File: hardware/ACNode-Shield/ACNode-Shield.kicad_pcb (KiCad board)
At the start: 2 copper layers, 50 x 50 mm, 15 parts, among them J1 MICRO_SD_HINGE, P1 CONN_NFC, P2 CONN_RELAY, P3 CONN_RGB_LED, P4 CONN_X6, P5 CONN_X7, P6 CONN_WS2812, Q1 PN2222A, SW1 SW_RST, SW2 SW_BTN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

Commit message: Rev 2 off to the fab
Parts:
- added CON1: SD_Card, SD_Slots:SD_Slot, F.Cu at (36.8, 49.5)
- C1: moved to F.Cu
- P2: footprint Pin_Headers:Pin_Header_Straight_1x03 -> Terminal_Blocks:TerminalBlock_Pheonix_MKDS1.5-3pol
- moved U2 11.8 mm to (58.0, 53.2), turned to 180 degrees
- moved P6 6.90 mm to (53.0, 54.0), turned to 180 degrees
- moved D1 6.41 mm to (32.0, 15.0)
- moved P2 5.78 mm to (15.0, 16.0), turned to 0 degrees
- moved C1 5.23 mm to (36.5, 40.0)
- moved U1 3.04 mm to (37.0, 29.5)
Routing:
- net +5V: track 129.1 -> 88.6 mm, vias 0 -> 1
- net PM7: track 17.1 -> 23.1 mm
- net PQ3: track 39.2 -> 44.8 mm, vias 0 -> 1
- net PQ1: track 41.3 -> 46.7 mm, vias 0 -> 1
- net PQ2: track 34.5 -> 39.5 mm, vias 0 -> 1
- net Net-(P2-Pad2): track 27.7 -> 22.9 mm
- net Net-(P6-Pad2): track 5.26 -> 9.67 mm
- net (no net): track 0.00 -> 3.17 mm
- net Net-(P2-Pad1): track 7.86 -> 10.9 mm
- net PQ0: track 31.7 -> 34.6 mm, vias 0 -> 2
- net Net-(D1-Pad2): track 29.9 -> 27.2 mm
- net +3.3v: track 52.4 -> 54.7 mm
- net GND: track 117.7 -> 119.5 mm, vias 0 -> 1
- net Net-(P2-Pad3): track 22.0 -> 21.1 mm
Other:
- board text added: "LHS ACNode Shield rev 2"
- board text removed: "LHS ACNode Shield rev 1"

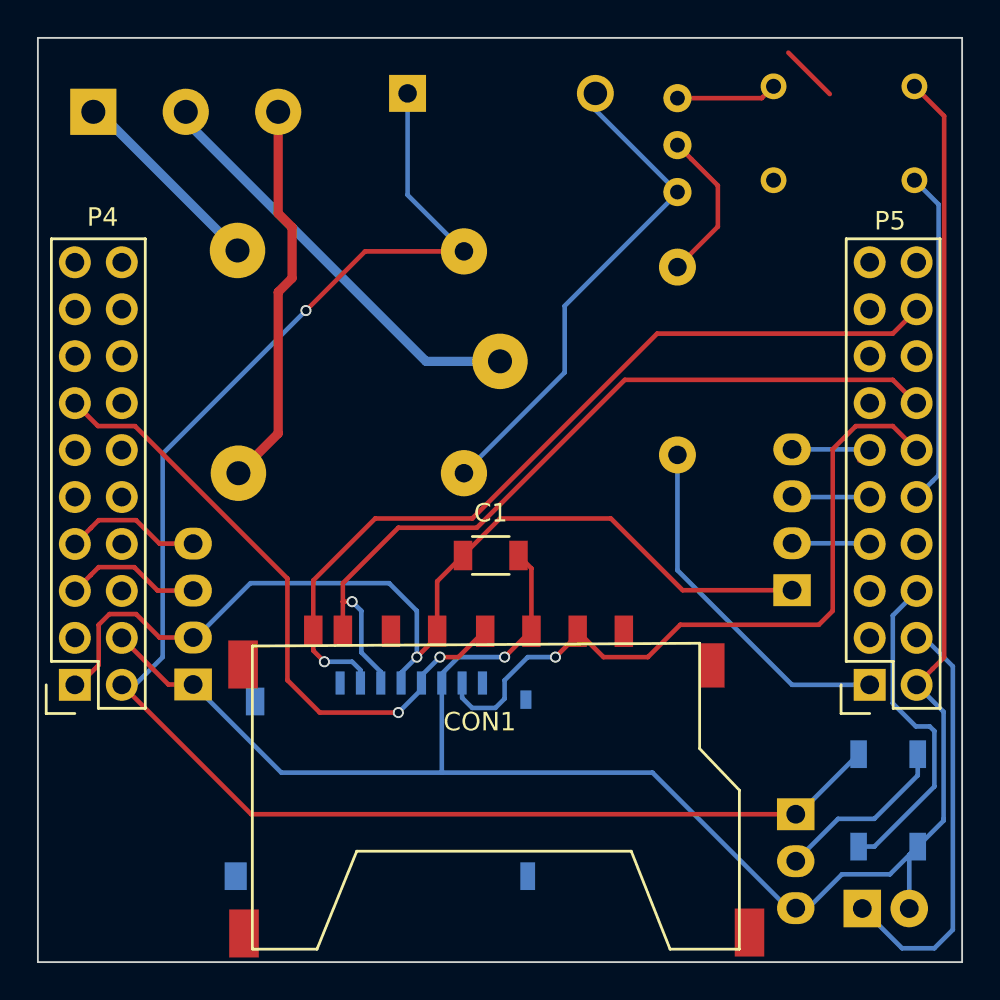
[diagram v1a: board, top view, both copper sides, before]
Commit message: Updated via outlines to be 1.2mm for easier manufacture.
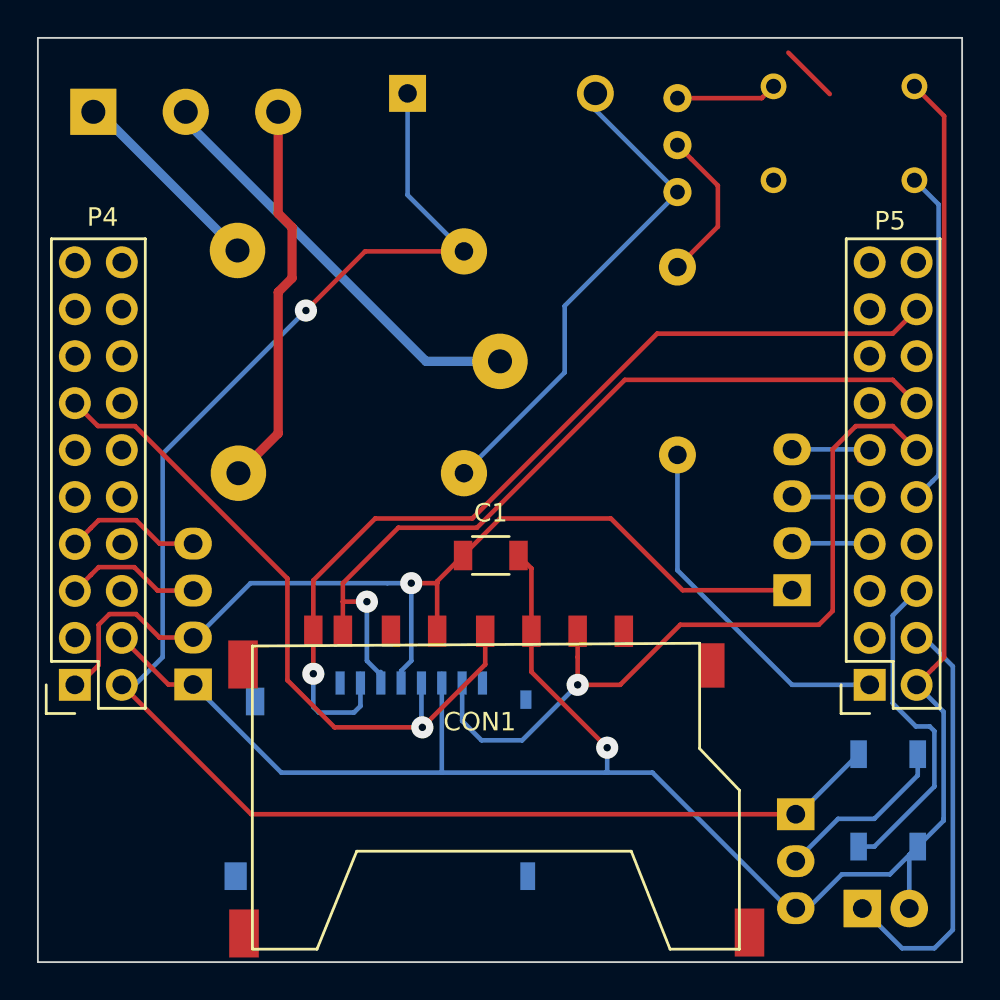
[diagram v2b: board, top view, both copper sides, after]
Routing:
- net PQ0: track 34.6 -> 39.1 mm, vias 2 -> 1
- net GND: track 119.5 -> 123.1 mm
- net PQ1: track 46.7 -> 50.2 mm
- net PQ2: track 39.5 -> 42.9 mm
- net PQ3: track 44.8 -> 46.3 mm
- net +3.3v: track 54.7 -> 55.6 mm
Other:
- net class Default: via_dia 0.6 -> 1.2

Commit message: Added some text on copper layers.
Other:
- board text added: "LHS"
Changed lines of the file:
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@@
     (links 45)
     (no_connects 2)
-    (area 11.949999 8.975 62.050001 65.175)
+    (area 11.949999 11.949999 62.050001 62.050001)
     (thickness 1.6)
-    (drawings 5)
+    (drawings 6)
     (tracks 204)
     (zones 0)
@@
     (pad "" smd rect (at -11.75 3.55) (size 1.3 2.4) (layers F.Cu F.Paste F.Mask))
   )
-  (gr_text "LHS\nACNode\nShield\nrev 2" (at 17.2 56.3) (layer B.SilkS)
+  (gr_text "LHS\nACNode\nShield\nrev 2" (at 17.4 56) (layer F.Cu)
+    (effects (font (size 1.5 1.5) (thickness 0.3)))
+  )
+  (gr_text LHS (at 42.2 60) (layer B.Cu)
     (effects (font (size 1.5 1.5) (thickness 0.3)) (justify mirror))
   )
@@
   (segment (start 52.6 12.8) (end 54.841001 15.041001) (width 0.25) (layer F.Cu) (net 0))
   (segment (start 32.2 41.5) (end 32.2 45.7) (width 0.25) (layer B.Cu) (net 1))
-  (segment (start 31.65 46.25) (end 31.65 46.9) (width 0.25) (layer B.Cu) (net 1) (status 800000))
+  (segment (start 31.65 46.25) (end 31.65 46.9) (width 0.25) (layer B.Cu) (net 1))
   (segment (start 32.2 45.7) (end 31.65 46.25) (width 0.25) (layer B.Cu) (net 1))
   (segment (start 30.9 41.5) (end 32.2 41.5) (width 0.25) (layer B.Cu) (net 1))
@@
   (segment (start 15.288601 45.924999) (end 14.2136 47) (width 0.25) (layer F.Cu) (net 1))
   (segment (start 14.2136 47) (end 14 47) (width 0.25) (layer F.Cu) (net 1))
-  (segment (start 38.7 44.1) (end 38.7 46.3) (width 0.25) (layer F.Cu) (net 2) (status 400000))
+  (segment (start 38.7 44.1) (end 38.7 46.3) (width 0.25) (layer F.Cu) (net 2))
   (segment (start 42.8 50.4) (end 42.8 51.75) (width 0.25) (layer B.Cu) (net 2))
   (via (at 42.8 50.4) (size 1.2) (drill 0.4) (layers F.Cu B.Cu) (net 2))
@@
   (segment (start 58.25 33) (end 56.25 33) (width 0.25) (layer F.Cu) (net 6))
   (segment (start 43.5 47) (end 46.75 43.75) (width 0.25) (layer F.Cu) (net 6))
-  (segment (start 34.95 46.9) (end 34.95 48.95) (width 0.25) (layer B.Cu) (net 6) (status 400000))
+  (segment (start 34.95 46.9) (end 34.95 48.95) (width 0.25) (layer B.Cu) (net 6))
   (segment (start 41.2 47) (end 41.2 45.5) (width 0.25) (layer F.Cu) (net 6))
-  (segment (start 41.2 45.5) (end 41.2 44.1) (width 0.25) (layer F.Cu) (net 6) (status 800000))
+  (segment (start 41.2 45.5) (end 41.2 44.1) (width 0.25) (layer F.Cu) (net 6))
   (via (at 41.2 47) (size 1.2) (drill 0.4) (layers F.Cu B.Cu) (net 6))
   (segment (start 38.2 50) (end 41.2 47) (width 0.25) (layer B.Cu) (net 6))
@@
   (segment (start 15.25 33) (end 14.01 31.76) (width 0.25) (layer F.Cu) (net 7))
   (segment (start 28.05 49.3) (end 25.5 46.75) (width 0.25) (layer F.Cu) (net 7))
-  (segment (start 32.75 46.9) (end 32.75 49.25) (width 0.25) (layer B.Cu) (net 7) (status 400000))
-  (segment (start 36.2 45.9) (end 36.2 44.1) (width 0.25) (layer F.Cu) (net 7) (status 800000))
+  (segment (start 32.75 46.9) (end 32.75 49.25) (width 0.25) (layer B.Cu) (net 7))
+  (segment (start 36.2 45.9) (end 36.2 44.1) (width 0.25) (layer F.Cu) (net 7))
   (segment (start 32.8 49.3) (end 36.2 45.9) (width 0.25) (layer F.Cu) (net 7))
   (via (at 32.8 49.3) (size 1.2) (drill 0.4) (layers F.Cu B.Cu) (net 7))
@@
   (via (at 29.8 42.5) (size 1.2) (drill 0.4) (layers F.Cu B.Cu) (net 8))
   (segment (start 28.5 42.5) (end 29.8 42.5) (width 0.25) (layer F.Cu) (net 8))
-  (segment (start 29.8 45.7) (end 30.55 46.45) (width 0.25) (layer B.Cu) (net 8) (status 800000))
-  (segment (start 30.55 46.45) (end 30.55 46.9) (width 0.25) (layer B.Cu) (net 8) (status C00000))
-  (segment (start 30.55 46.9) (end 30.55 46.45) (width 0.25) (layer B.Cu) (net 8) (status C00000))
+  (segment (start 29.8 45.7) (end 30.55 46.45) (width 0.25) (layer B.Cu) (net 8))
+  (segment (start 30.55 46.45) (end 30.55 46.9) (width 0.25) (layer B.Cu) (net 8))
+  (segment (start 30.55 46.9) (end 30.55 46.45) (width 0.25) (layer B.Cu) (net 8))
   (segment (start 59.54 31.76) (end 59.51 31.76) (width 0.25) (layer F.Cu) (net 8))
   (segment (start 59.51 31.76) (end 58.25 30.5) (width 0.25) (layer F.Cu) (net 8))
@@
   (segment (start 28.5 42.5) (end 28.5 44.1) (width 0.25) (layer F.Cu) (net 8))
   (segment (start 30.55 46.9) (end 30.55 46.4) (width 0.25) (layer B.Cu) (net 8))
-  (segment (start 29.45 46.9) (end 29.45 48.15) (width 0.25) (layer B.Cu) (net 9) (status 400000))
-  (segment (start 26.9 46.4) (end 26.9 44.1) (width 0.25) (layer F.Cu) (net 9) (status 800000))
+  (segment (start 29.45 46.9) (end 29.45 48.15) (width 0.25) (layer B.Cu) (net 9))
+  (segment (start 26.9 46.4) (end 26.9 44.1) (width 0.25) (layer F.Cu) (net 9))
   (via (at 26.9 46.4) (size 1.2) (drill 0.4) (layers F.Cu B.Cu) (net 9))
   (segment (start 26.9 48.2) (end 26.9 46.4) (width 0.25) (layer B.Cu) (net 9))

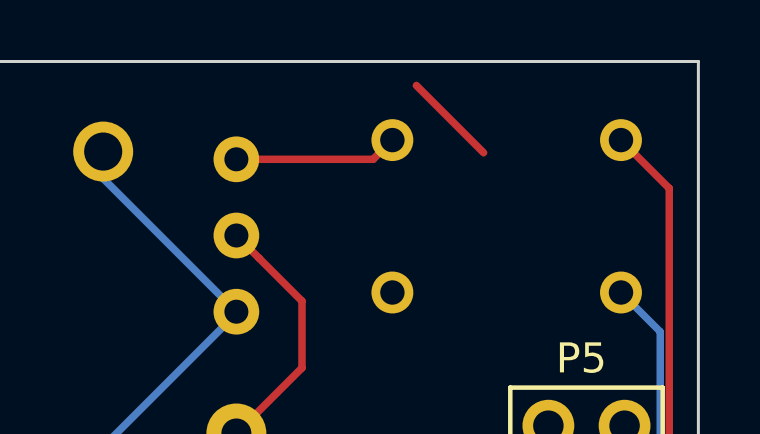
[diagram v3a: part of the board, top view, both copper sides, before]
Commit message: Removed a single trace that wasn't needed.
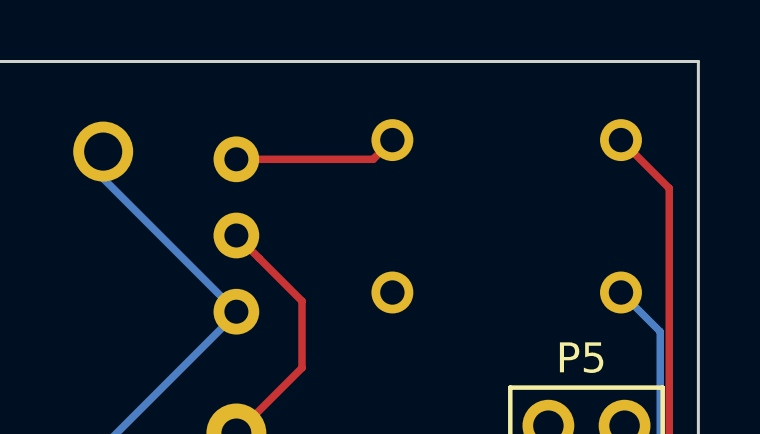
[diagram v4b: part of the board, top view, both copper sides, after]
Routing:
- net (no net): track 3.17 -> 0.00 mm
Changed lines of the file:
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@@
     (links 45)
     (no_connects 2)
-    (area 11.949999 11.949999 62.050001 62.050001)
+    (area 11.949999 8.975 62.050001 65.175)
     (thickness 1.6)
     (drawings 6)
-    (tracks 204)
+    (tracks 203)
     (zones 0)
     (modules 16)
@@
   (gr_line (start 62 12) (end 62 62) (layer Edge.Cuts) (width 0.1))
   (gr_line (start 12 12) (end 62 12) (layer Edge.Cuts) (width 0.1))
-  (segment (start 52.6 12.8) (end 54.841001 15.041001) (width 0.25) (layer F.Cu) (net 0))
   (segment (start 32.2 41.5) (end 32.2 45.7) (width 0.25) (layer B.Cu) (net 1))
   (segment (start 31.65 46.25) (end 31.65 46.9) (width 0.25) (layer B.Cu) (net 1))

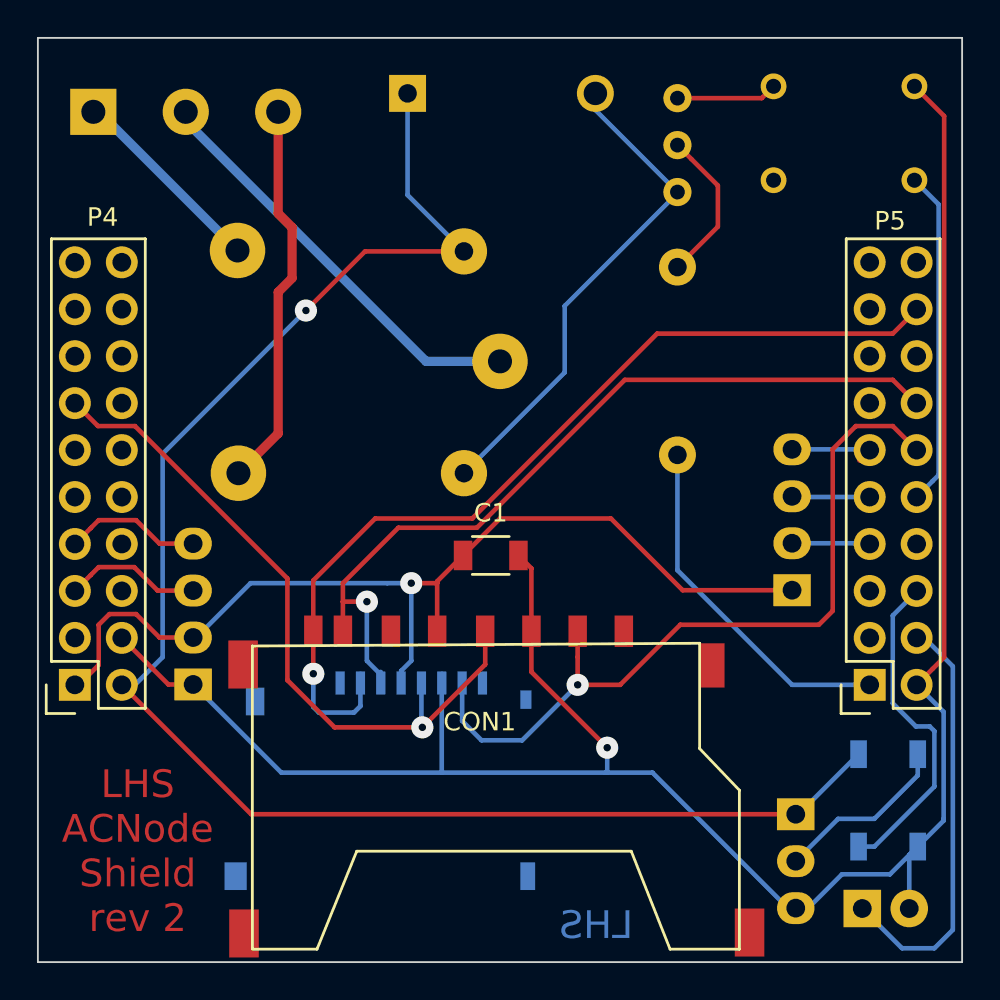
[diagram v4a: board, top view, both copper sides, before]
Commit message: Removed large SD card connector - it doesn't fit.
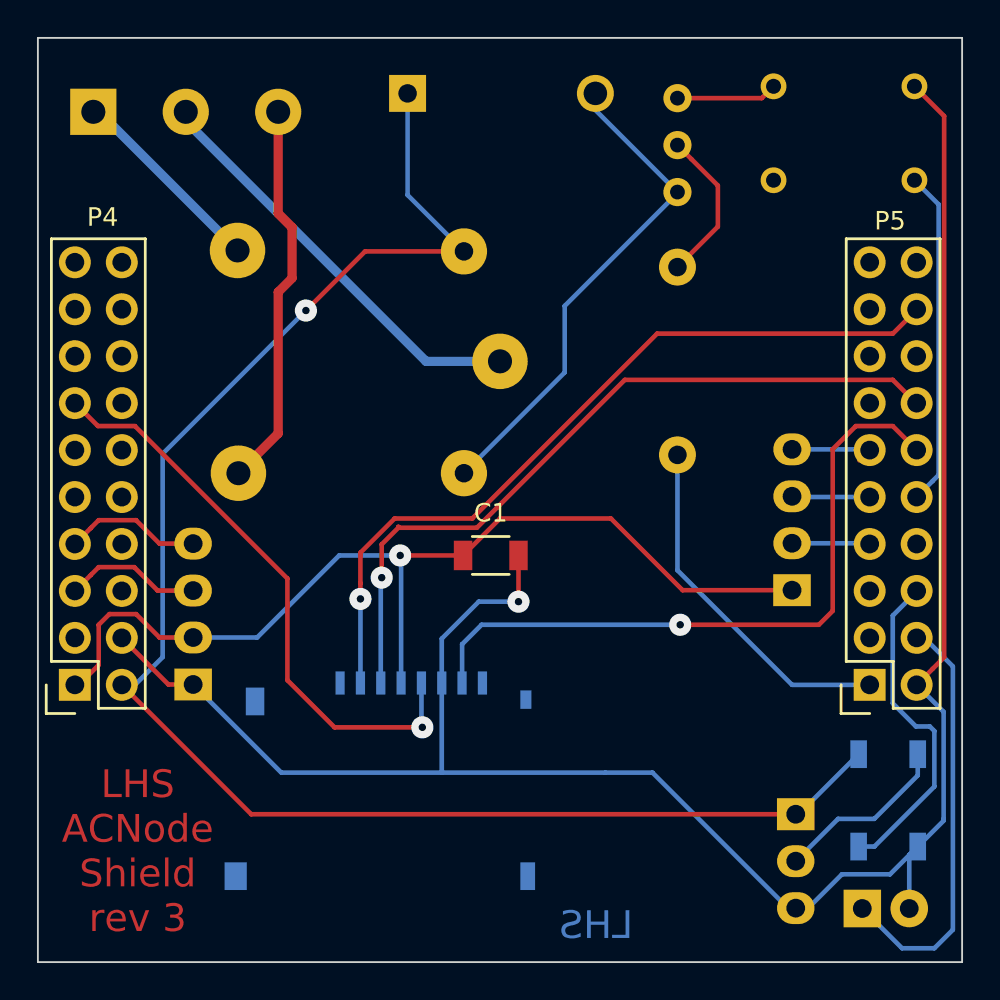
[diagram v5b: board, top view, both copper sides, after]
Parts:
- removed CON1: SD_Card, SD_Slots:SD_Slot
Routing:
- net PQ1: track 50.2 -> 43.1 mm
- net PQ0: track 39.1 -> 32.5 mm
- net PQ2: track 42.9 -> 37.2 mm
- net PQ3: track 46.3 -> 42.2 mm
- net GND: track 123.1 -> 119.2 mm
- net +3.3v: track 55.6 -> 54.1 mm
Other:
- board text added: "LHS ACNode Shield rev 3"
- board text removed: "LHS ACNode Shield rev 2"

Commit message: Copper fill. Regenerated gerbers.
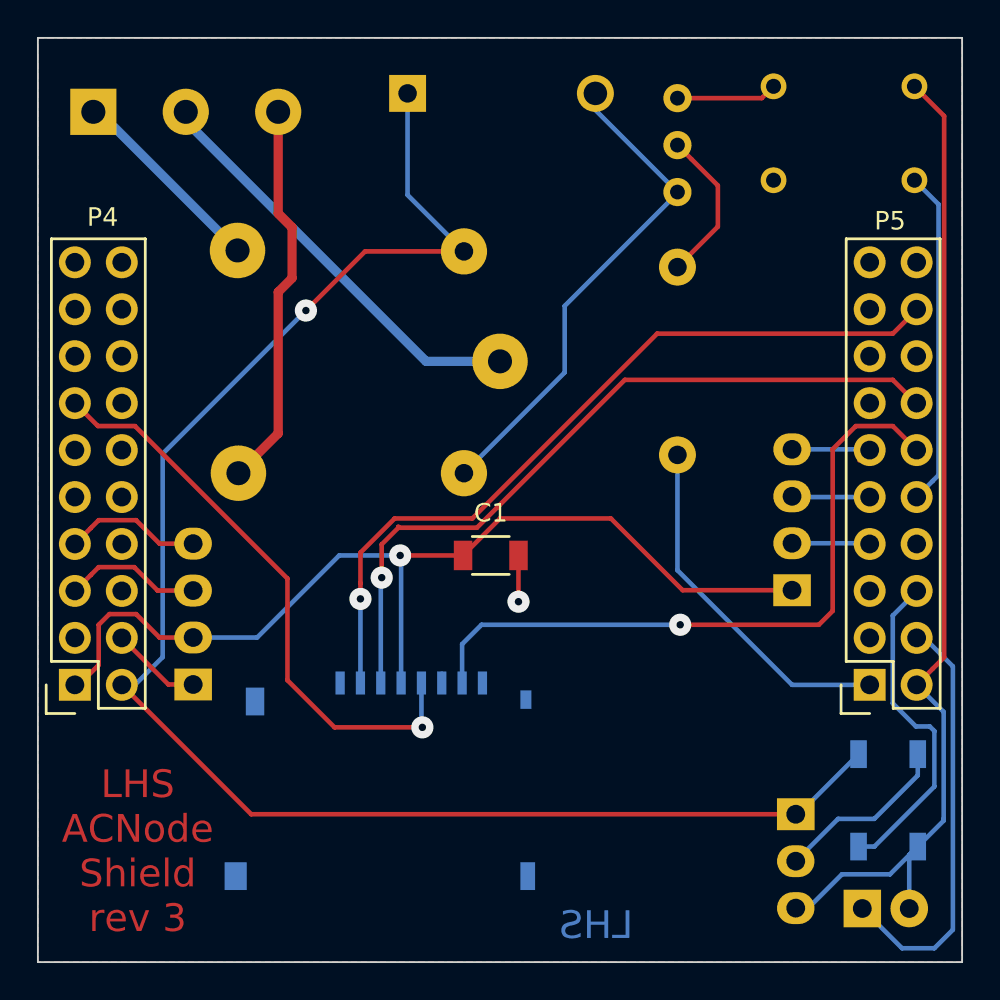
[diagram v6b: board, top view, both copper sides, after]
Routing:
- net GND: track 119.2 -> 69.8 mm
- added copper zone on B.Cu, net GND
- added copper zone on F.Cu, net GND
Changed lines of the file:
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@@
   (general
     (links 39)
-    (no_connects 2)
+    (no_connects 1)
     (area 11.949999 11.949999 62.050001 62.050001)
     (thickness 1.6)
     (drawings 6)
-    (tracks 183)
+    (tracks 174)
     (zones 0)
     (modules 15)
@@
   (segment (start 15.288601 45.924999) (end 14.2136 47) (width 0.25) (layer F.Cu) (net 1))
   (segment (start 14.2136 47) (end 14 47) (width 0.25) (layer F.Cu) (net 1))
-  (segment (start 33.85 46.9) (end 33.85 44.5) (width 0.25) (layer B.Cu) (net 2) (status 400000))
-  (segment (start 38 42.5) (end 38 40) (width 0.25) (layer F.Cu) (net 2) (status 800000))
+  (segment (start 38 42.5) (end 38 40) (width 0.25) (layer F.Cu) (net 2))
   (via (at 38 42.5) (size 1.2) (drill 0.4) (layers F.Cu B.Cu) (net 2))
-  (segment (start 35.85 42.5) (end 38 42.5) (width 0.25) (layer B.Cu) (net 2))
-  (segment (start 33.85 44.5) (end 35.85 42.5) (width 0.25) (layer B.Cu) (net 2))
-  (segment (start 33.85 46.9) (end 33.85 51.75) (width 0.25) (layer B.Cu) (net 2))
   (segment (start 33.85 46.9) (end 33.85 46.4) (width 0.25) (layer B.Cu) (net 2))
   (segment (start 53 59.08) (end 52.58 59.08) (width 0.25) (layer B.Cu) (net 2))
-  (segment (start 52.58 59.08) (end 45.25 51.75) (width 0.25) (layer B.Cu) (net 2))
-  (segment (start 45.25 51.75) (end 42.7 51.75) (width 0.25) (layer B.Cu) (net 2))
-  (segment (start 42.7 51.75) (end 33.85 51.75) (width 0.25) (layer B.Cu) (net 2))
-  (segment (start 25.17 51.75) (end 20.4 46.98) (width 0.25) (layer B.Cu) (net 2))
-  (segment (start 33.85 51.75) (end 25.17 51.75) (width 0.25) (layer B.Cu) (net 2))
   (segment (start 59.14 59.1) (end 59.14 56.20956) (width 0.25) (layer B.Cu) (net 2))
   (segment (start 59.14 56.20956) (end 59.6002 55.74936) (width 0.25) (layer B.Cu) (net 2))
@@
   (segment (start 53 54) (end 53.15044 54) (width 0.25) (layer B.Cu) (net 4))
   (segment (start 53.15044 54) (end 56.3998 50.75064) (width 0.25) (layer B.Cu) (net 4))
-  (segment (start 34.95 46.9) (end 34.95 44.8) (width 0.25) (layer B.Cu) (net 6) (status 400000))
+  (segment (start 34.95 46.9) (end 34.95 44.8) (width 0.25) (layer B.Cu) (net 6))
   (segment (start 58.25 33) (end 56.25 33) (width 0.25) (layer F.Cu) (net 6))
   (segment (start 56.25 33) (end 55 34.25) (width 0.25) (layer F.Cu) (net 6))
@@
   (segment (start 48.787001 19.987001) (end 47.361999 18.561999) (width 0.25) (layer F.Cu) (net 47))
   (segment (start 47.361999 18.561999) (end 46.6 17.8) (width 0.25) (layer F.Cu) (net 47))
+  (zone (net 2) (net_name GND) (layer F.Cu) (hatch edge 0.508)
+    (connect_pads (clearance 0.508))
+    (min_thickness 0.254)
+    (fill yes (arc_segments 16) (thermal_gap 0.508) (thermal_bridge_width 0.508))
+    (polygon
+      (pts
+        (xy 12 12) (xy 62 12) (xy 62 62) (xy 12 62)
+      )
+    )
+  )
+  (zone (net 2) (net_name GND) (layer B.Cu) (hatch edge 0.508)
+    (connect_pads (clearance 0.508))
+    (min_thickness 0.254)
+    (fill yes (arc_segments 16) (thermal_gap 0.508) (thermal_bridge_width 0.508))
+    (polygon
+      (pts
+        (xy 12 12) (xy 62 12) (xy 62 62) (xy 12 62)
+      )
+    )
+  )
 )
